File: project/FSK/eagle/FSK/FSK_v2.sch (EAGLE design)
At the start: 31 parts, among them IC1 74AUC1G32DCK, X1 SMA-142-0711-821/826, X2 SMA-142-0711-821/826, X3 SMA-142-0711-821/826, X4 SMA-142-0711-821/826, X5 SMA-142-0711-821/826, X6 22-23-2021

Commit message: updates to FSK board
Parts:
- removed LED1: S4301B, led-7-segment:S4301B
- added C4, C5: (no value), rcl:C-USC0603
- added R11, R12, R13, R14, R15, R16, R17: (no value), rcl:R-US_R0603
- added U$11: 7S_DISPLAY, ECE532_Parts:7S_DISPLAY
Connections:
- removed net AGND: IC1P.GND, U$5.IND+, U$5.IND-
- new net N$20: R14.1, U$4.D
- new net N$21: R15.1, U$4.E
- new net N$22: R16.1, U$4.F
- new net N$23: R17.1, U$4.G
- new net N$3: R11.2, U$11.A
- new net N$4: R12.2, U$11.B
- new net N$7: R13.2, U$11.C
- net GND1: now also C4.2, C5.2, IC1P.GND, U$11.C@1, U$11.C@2, U$5.IND+, U$5.IND-; no longer LED1.C@1, LED1.C@2
- net N$13: now also R14.2, U$11.D; no longer LED1.E, U$4.E
- net N$14: now also R15.2, U$11.E; no longer LED1.D, U$4.D
- net N$15: now also R16.2, U$11.F; no longer LED1.C, U$4.C
- net N$16: now also R17.2, U$11.G; no longer LED1.B, U$4.B
- net N$17: now also R11.1; no longer LED1.A
- net N$18: now also R12.1, U$4.B; no longer LED1.G, U$4.G
- net N$19: now also R13.1, U$4.C; no longer LED1.F, U$4.F
- net VCC: now also C4.1, C5.1

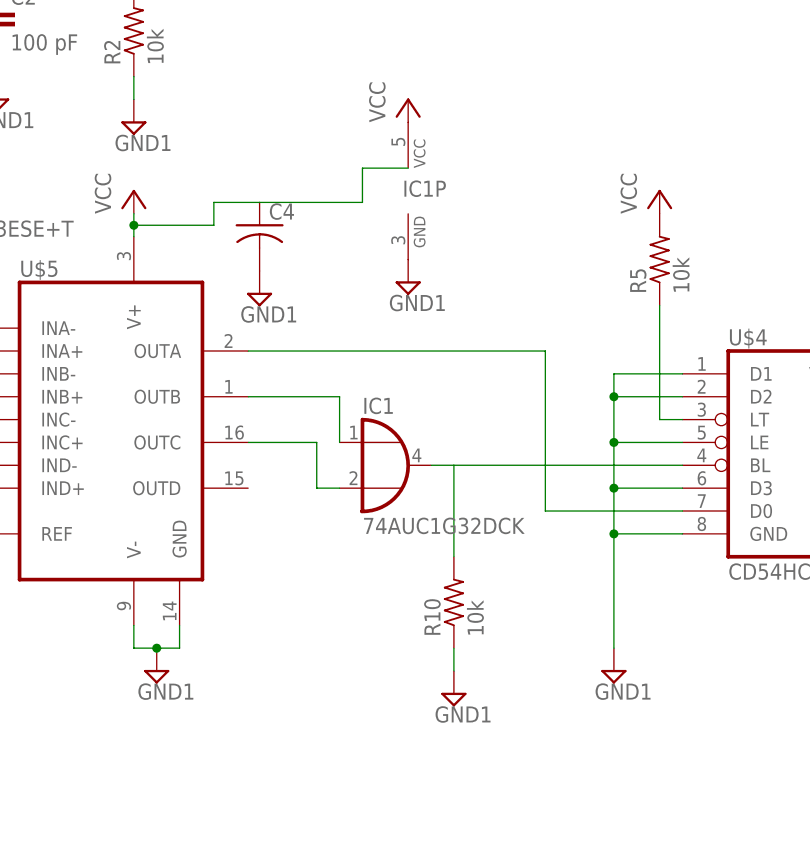
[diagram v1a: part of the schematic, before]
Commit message: added final schem for FSK board and gerbers
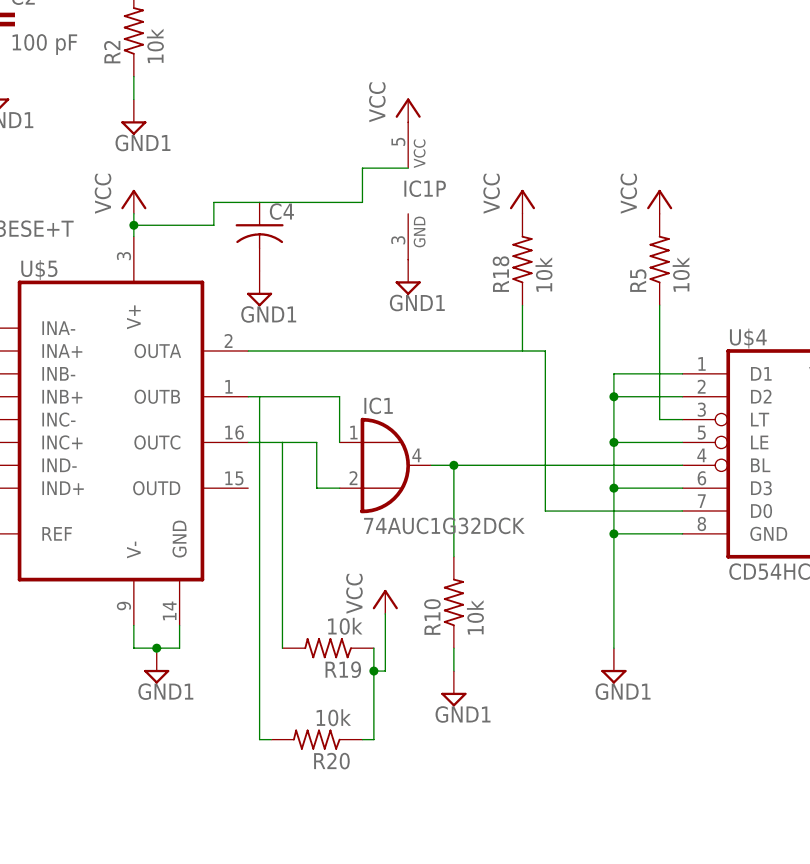
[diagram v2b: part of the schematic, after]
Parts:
- added R18, R19, R20: 10k, rcl:R-US_R1206
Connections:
- net N$2: now also R20.2
- net N$6: now also R18.1
- net N$8: now also R19.2
- net VCC: now also R18.2, R19.1, R20.1
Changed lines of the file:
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@@
 <part name="SUPPLY16" library="supply2" deviceset="GND1" device=""/>
 <part name="SUPPLY9" library="supply2" deviceset="GND1" device=""/>
+<part name="R18" library="rcl" deviceset="R-US_" device="R1206" value="10k"/>
+<part name="R19" library="rcl" deviceset="R-US_" device="R1206" value="10k"/>
+<part name="R20" library="rcl" deviceset="R-US_" device="R1206" value="10k"/>
+<part name="P+6" library="supply1" deviceset="VCC" device=""/>
+<part name="P+7" library="supply1" deviceset="VCC" device=""/>
 </parts>
 <sheets>
@@
 <instance part="SUPPLY16" gate="G$1" x="347.98" y="83.82"/>
 <instance part="SUPPLY9" gate="G$1" x="226.06" y="66.04"/>
+<instance part="R18" gate="G$1" x="294.64" y="93.98" rot="R90"/>
+<instance part="R19" gate="G$1" x="273.05" y="50.8" rot="R180"/>
+<instance part="R20" gate="G$1" x="271.78" y="40.64" rot="R180"/>
+<instance part="P+6" gate="VCC" x="279.4" y="57.15"/>
+<instance part="P+7" gate="VCC" x="294.64" y="101.6"/>
 </instances>
 <busses>
@@
 <wire x1="287.02" y1="71.12" x2="284.48" y2="71.12" width="0.1524" layer="91"/>
 <wire x1="287.02" y1="60.96" x2="287.02" y2="71.12" width="0.1524" layer="91"/>
+<junction x="287.02" y="71.12"/>
 </segment>
 </net>
@@
 <wire x1="297.18" y1="66.04" x2="312.42" y2="66.04" width="0.1524" layer="91"/>
 <pinref part="U$5" gate="G$1" pin="OUTA"/>
-<wire x1="297.18" y1="83.82" x2="264.16" y2="83.82" width="0.1524" layer="91"/>
+<wire x1="297.18" y1="83.82" x2="294.64" y2="83.82" width="0.1524" layer="91"/>
+<pinref part="R18" gate="G$1" pin="1"/>
+<wire x1="294.64" y1="83.82" x2="264.16" y2="83.82" width="0.1524" layer="91"/>
+<wire x1="294.64" y1="83.82" x2="294.64" y2="88.9" width="0.1524" layer="91"/>
 </segment>
 </net>
@@
 <wire x1="281.94" y1="149.86" x2="284.48" y2="149.86" width="0.1524" layer="91"/>
 </segment>
+<segment>
+<pinref part="P+6" gate="VCC" pin="VCC"/>
+<wire x1="279.4" y1="54.61" x2="279.4" y2="48.26" width="0.1524" layer="91"/>
+<wire x1="279.4" y1="48.26" x2="278.13" y2="48.26" width="0.1524" layer="91"/>
+<pinref part="R20" gate="G$1" pin="1"/>
+<pinref part="R19" gate="G$1" pin="1"/>
+<wire x1="276.86" y1="40.64" x2="278.13" y2="40.64" width="0.1524" layer="91"/>
+<wire x1="278.13" y1="40.64" x2="278.13" y2="48.26" width="0.1524" layer="91"/>
+<junction x="278.13" y="48.26"/>
+<wire x1="278.13" y1="48.26" x2="278.13" y2="50.8" width="0.1524" layer="91"/>
+</segment>
+<segment>
+<pinref part="R18" gate="G$1" pin="2"/>
+<pinref part="P+7" gate="VCC" pin="VCC"/>
+</segment>
 </net>
 <net name="N$2" class="0">
@@
 <wire x1="274.32" y1="73.66" x2="274.32" y2="78.74" width="0.1524" layer="91"/>
 <pinref part="U$5" gate="G$1" pin="OUTB"/>
-<wire x1="274.32" y1="78.74" x2="264.16" y2="78.74" width="0.1524" layer="91"/>
+<wire x1="274.32" y1="78.74" x2="265.43" y2="78.74" width="0.1524" layer="91"/>
+<wire x1="265.43" y1="78.74" x2="264.16" y2="78.74" width="0.1524" layer="91"/>
+<wire x1="265.43" y1="78.74" x2="265.43" y2="40.64" width="0.1524" layer="91"/>
+<pinref part="R20" gate="G$1" pin="2"/>
+<wire x1="265.43" y1="40.64" x2="266.7" y2="40.64" width="0.1524" layer="91"/>
 </segment>
 </net>
@@
 <wire x1="271.78" y1="68.58" x2="271.78" y2="73.66" width="0.1524" layer="91"/>
 <pinref part="U$5" gate="G$1" pin="OUTC"/>
-<wire x1="271.78" y1="73.66" x2="264.16" y2="73.66" width="0.1524" layer="91"/>
-</segment>
-</net>
+<wire x1="271.78" y1="73.66" x2="267.97" y2="73.66" width="0.1524" layer="91"/>
+<pinref part="R19" gate="G$1" pin="2"/>
+<wire x1="267.97" y1="73.66" x2="264.16" y2="73.66" width="0.1524" layer="91"/>
+<wire x1="267.97" y1="73.66" x2="267.97" y2="50.8" width="0.1524" layer="91"/>
+</segment>
+</net>
